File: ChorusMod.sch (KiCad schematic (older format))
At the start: 112 parts, among them J1 AuxAudioIn, J1.11 WT, J1.12 BK, J1.13 OR, J1.14 YL, J1.15 OR+BK, J1.16 YL+BK, J1.17 GN, J2.1 BN, J2.2 RD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

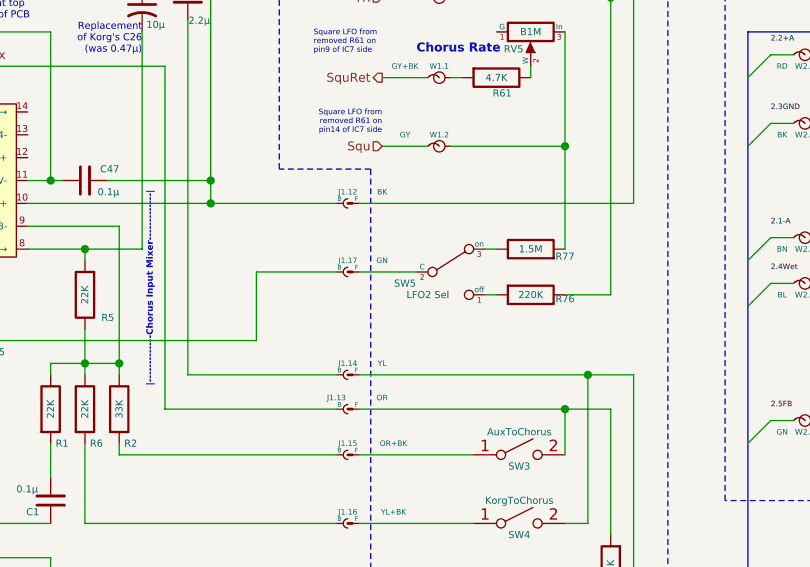
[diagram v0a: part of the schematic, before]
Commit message: save point after modding my Korg. Next: replace wire colors with meaningful labels others can follow
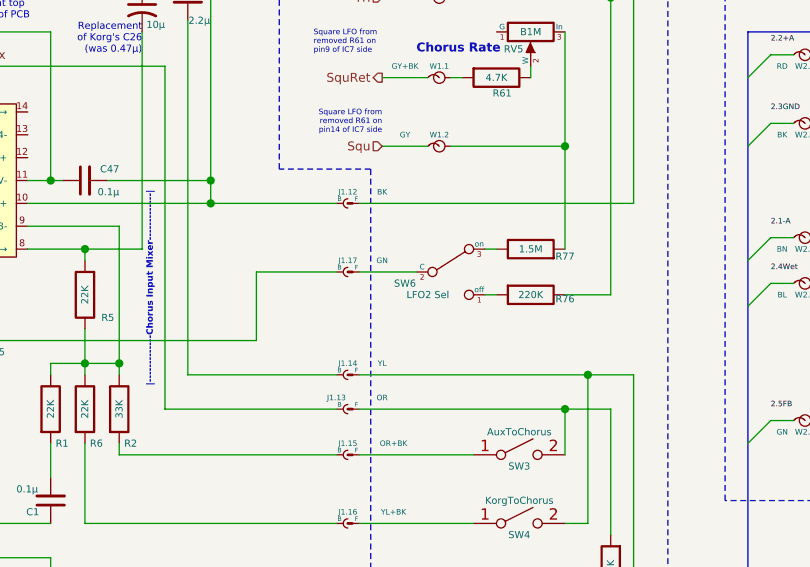
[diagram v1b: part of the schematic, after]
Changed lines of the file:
@@
 AR Path="/5A11371F/59F86E70" Ref="SW5"  Part="1"
 AR Path="/59FAABE9/59FAB4E6/59F86E70" Ref="SW5"  Part="1"
-F 0 "SW5" H 5150 2700 31  0000 C CNN
+F 0 "SW6" H 5150 2700 31  0000 C CNN
 F 1 "LFO2 Sel" H 5250 2650 31  0000 C CNN
 F 2 "MyKi_TH_Panel_Controls:TH_SPDT_Angled" H 5350 2750 50  0001 C CNN
